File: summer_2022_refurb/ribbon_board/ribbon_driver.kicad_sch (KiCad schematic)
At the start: 9 parts

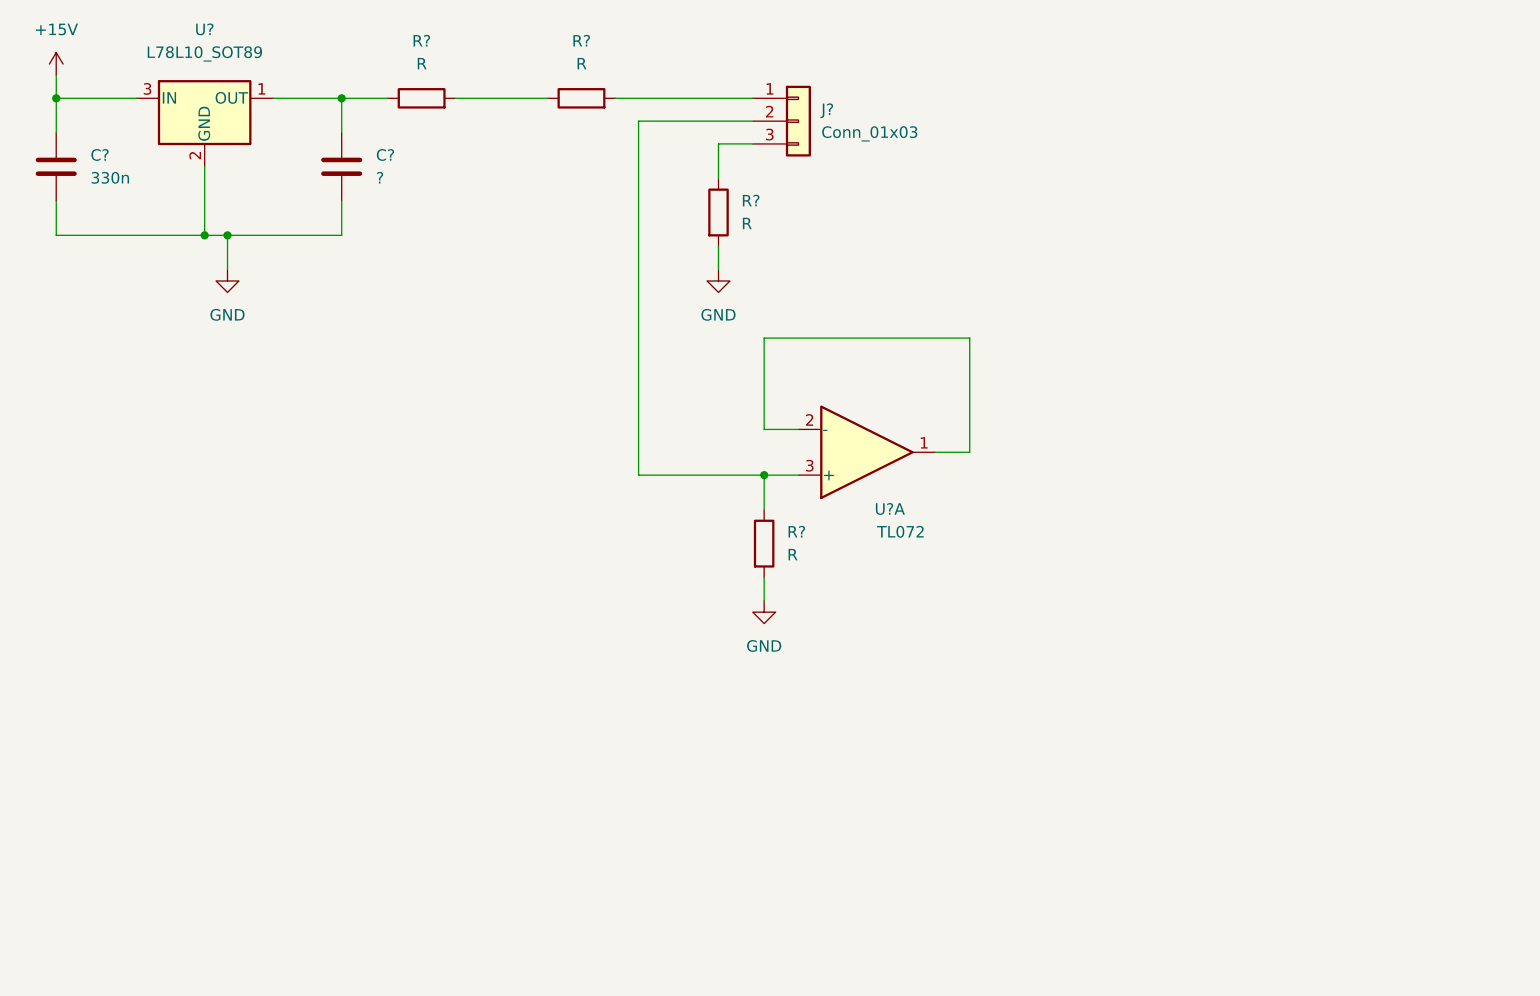
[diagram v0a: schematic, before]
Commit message: Progress on ribbon board
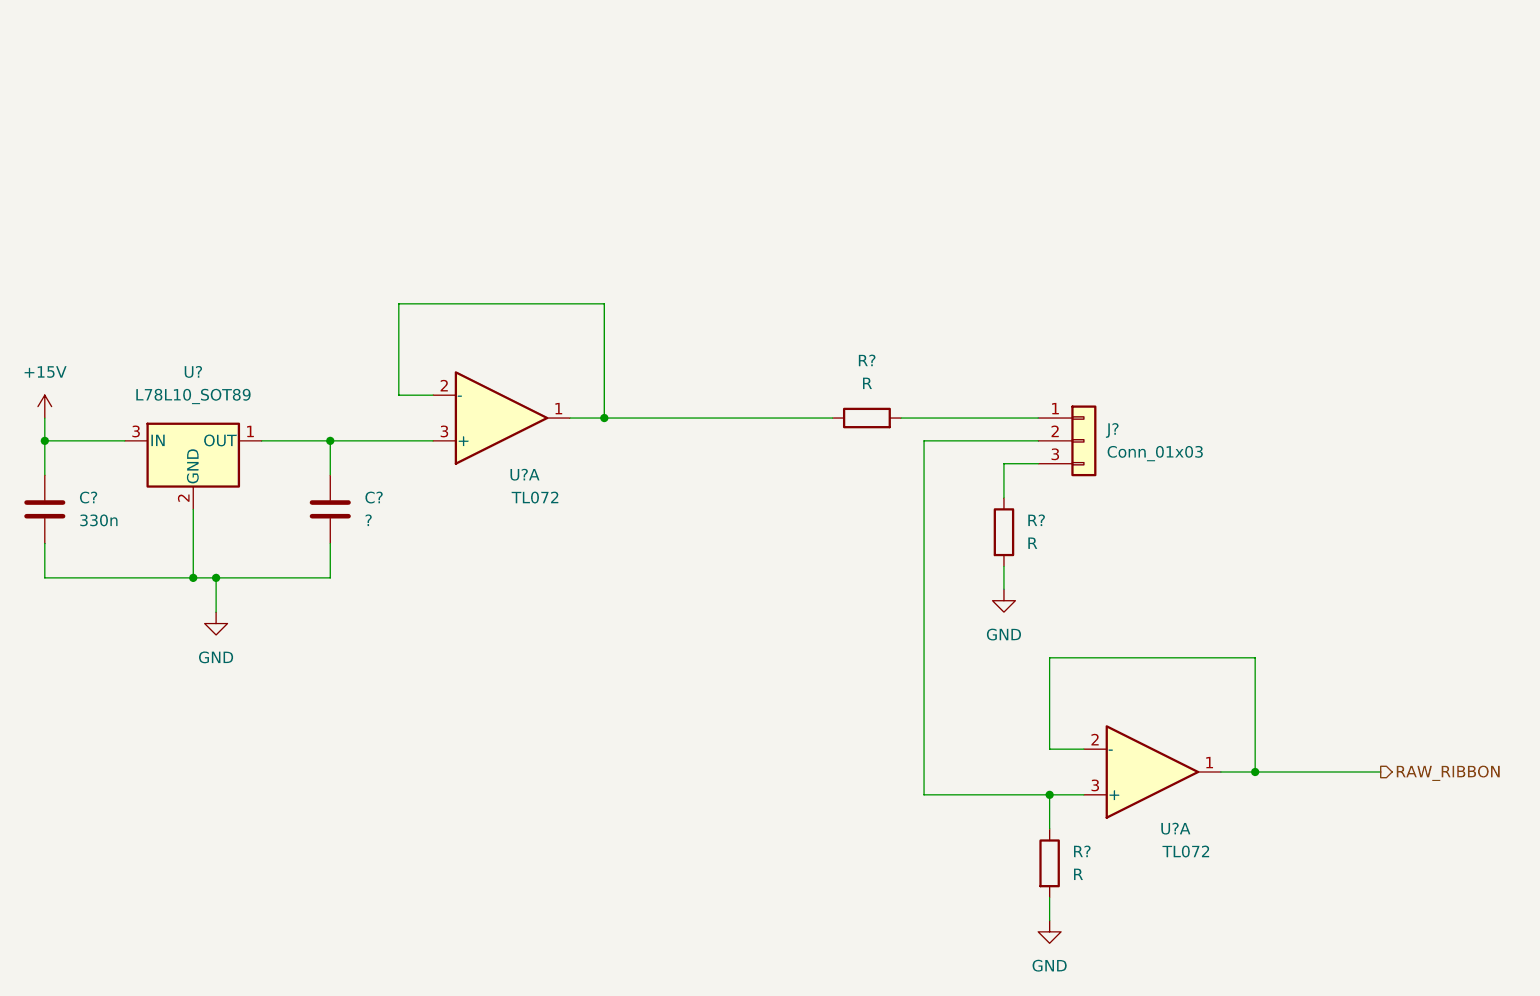
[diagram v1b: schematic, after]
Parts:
- removed R?: R, symbol Device:R
- added U?: TL072, symbol Amplifier_Operational:TL072
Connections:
- net at C?.1, U?.1 (OUT): now also U?.3 (+); no longer R?.1
- net at R?.2: now also J?.1 (Pin_1)
- net RAW_RIBBON: now reaches U?.1, U?.2 (-)
- new net: R?.1, U?.1, U?.2 (-)
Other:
- moved on the sheet: C?, J?, R?, U?, U?A

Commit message: Ribbon board progress, tidy up schem
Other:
- title: (none) -> Josh Ox Ribbon Synth Ribbon board
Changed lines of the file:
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@@
 (kicad_sch (version 20211123) (generator eeschema)
   (paper "A4")
+  (title_block
+    (title "Josh Ox Ribbon Synth Ribbon board")
+    (date "2022-06-16")
+    (rev "0")
+    (comment 1 "creativecommons.org/licences/by/4.0")
+    (comment 2 "license: CC by 4.0")
+    (comment 3 "Author: Jordan Aceto")
+  )
   (junction (at 101.6 101.6) (diameter 0) (color 0 0 0 0)
   )
